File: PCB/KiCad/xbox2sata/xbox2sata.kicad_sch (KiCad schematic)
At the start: 47 parts, among them J1 929975-01-20-RK, J2 61203921621, J3 SATA-A-PL-SMT-K, U1 1V2 voltage regulator, U5 88SA8052, Y1 25MHz

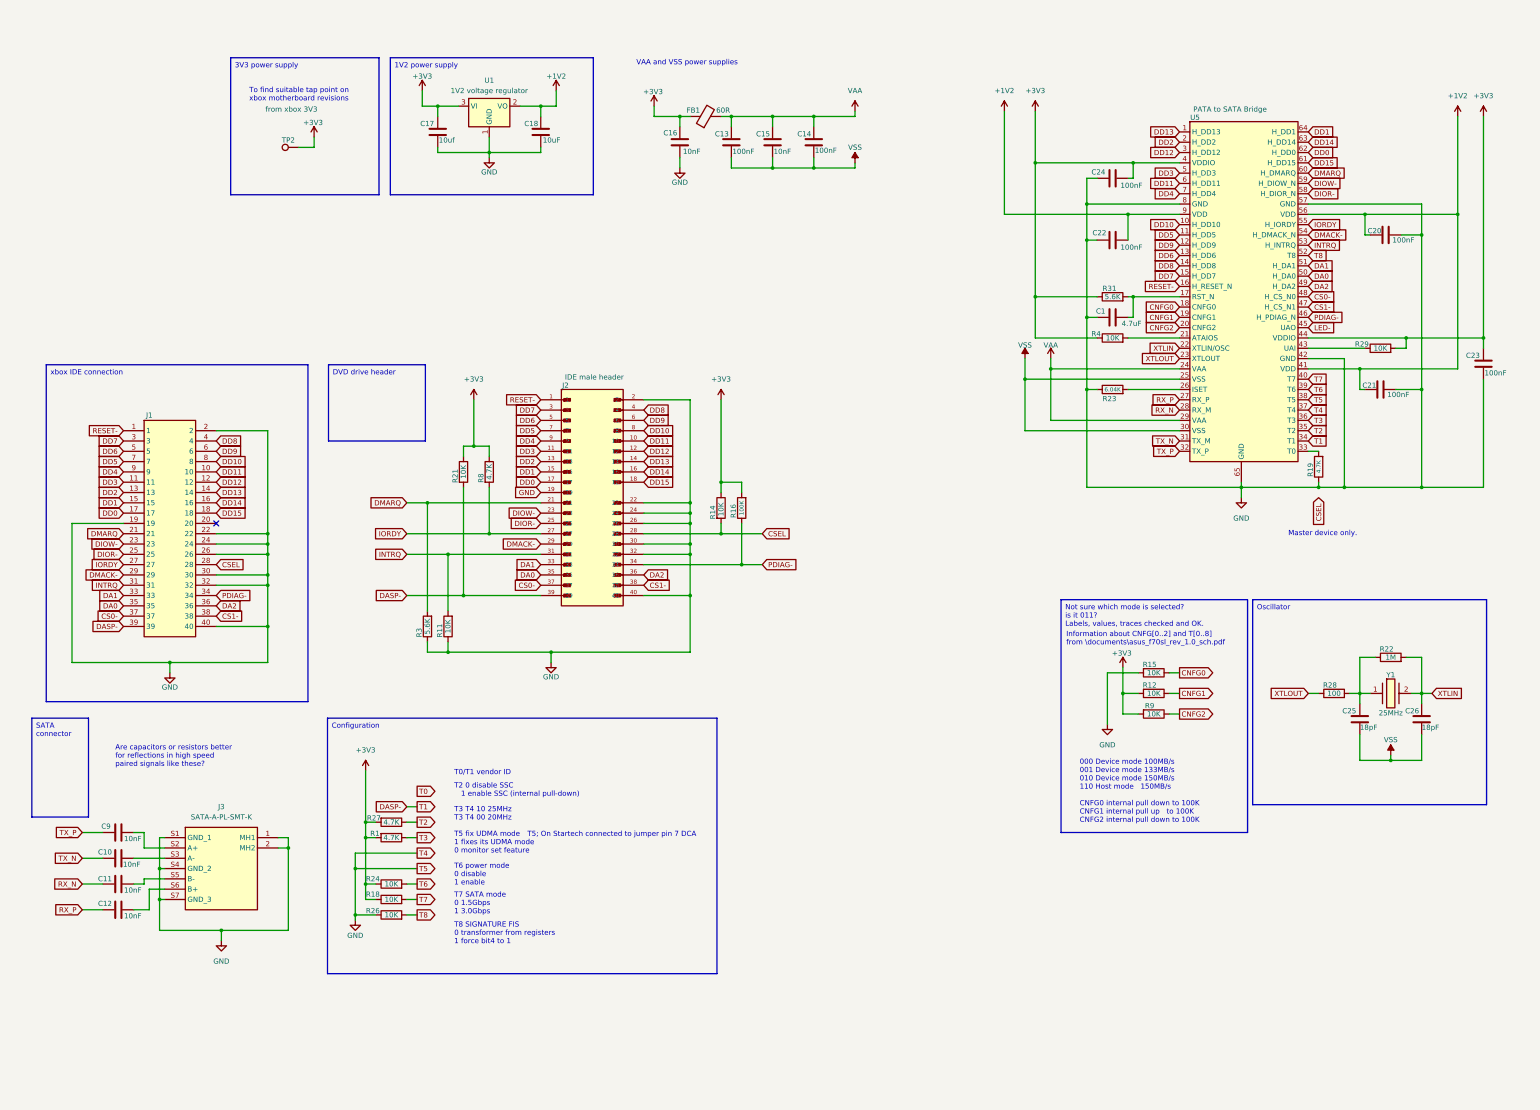
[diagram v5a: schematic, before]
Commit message: Reset-Negative was not enabled
10K resistor (R14) pull-up to 3V3 added to CSEL IDE pin 28
4.7K resistor (R19) pull-down to ground on T0 U5 pin 33 to device as IDE master
Positive power supply icons changed from Global labels to Power symbols

Via sizes changed to 0.3 and 0.5 mm for jlcpcb requirements
Bill of materials updated
Mouser shared basket created;
https://www.mouser.co.uk/api/CrossDomain/GetContext?syncDomains=www&returnUrl=https%3a%2f%2fwww.mouser.com%2fProjectManager%2fProjectDetail.aspx%3fAccessID%3da2276a8976&async=False&setPrefSub=False&clearPrefSub=False
Datasheets added
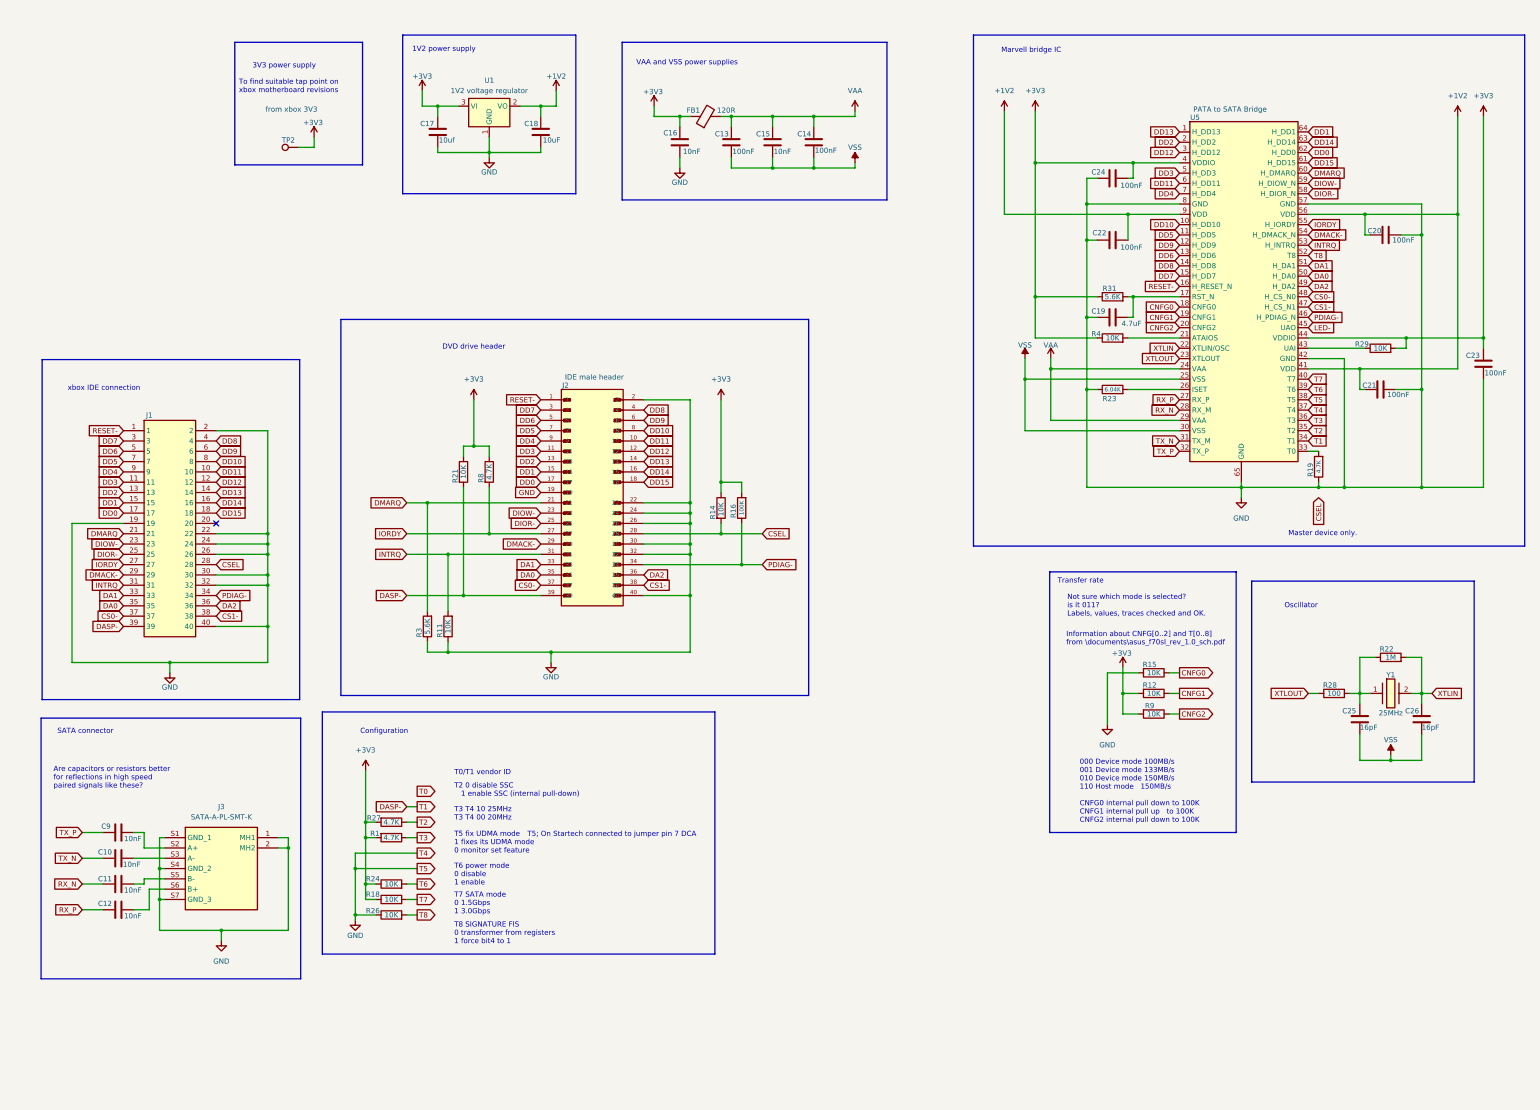
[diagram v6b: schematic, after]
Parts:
- C10, C11, C12, C9: footprint Resistor_SMD:R_0402_1005Metric_Pad0.72x0.64mm_HandSolder -> Capacitor_SMD:C_0402_1005Metric_Pad0.74x0.62mm_HandSolder
- C17, C18: footprint Capacitor_SMD:C_0603_1608Metric_Pad1.08x0.95mm_HandSolder -> Capacitor_SMD:C_0805_2012Metric
- C25, C26: value 18pF -> 16pF
- FB1: value 60R -> 120R; footprint Resistor_SMD:R_0402_1005Metric_Pad0.72x0.64mm_HandSolder -> Inductor_SMD:L_0603_1608Metric; Current rating (none) -> 2A; Frequency (none) -> 100Mhz
- renumbered C1 to C19
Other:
- note added: "1V2 power supply"
- note added: "3V3 power supply"
- note added: "Configuration"
- note added: "DVD drive header"
- note added: "Marvell bridge IC"
- note added: "Not sure which mode is selected? is it 011? Labels, values, traces checked and OK."
- note added: "Oscillator"
- note added: "SATA connector"
- note added: "Transfer rate"
- note added: "xbox IDE connection"
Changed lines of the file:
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@@
 		)
 	)
-	(text_box "Configuration"
-		(exclude_from_sim yes)
-		(at 103.632 187.706 0)
-		(size 96.012 62.992)
+	(rectangle
+		(start 33.274 99.314)
+		(end 96.774 183.134)
 		(stroke
 			(width 0)
@@
 			(type none)
 		)
-		(effects
-			(font
-				(face "Consolas")
-				(size 1.27 1.27)
-			)
-			(justify left top)
-		)
 	)
-	(text_box "1V2 power supply"
-		(exclude_from_sim no)
-		(at 119.126 24.892 0)
-		(size 50.038 33.782)
+	(rectangle
+		(start 331.47 153.924)
+		(end 386.334 203.454)
 		(stroke
 			(width 0)
@@
 			(type none)
 		)
-		(effects
-			(font
-				(face "Consolas")
-				(size 1.27 1.27)
-			)
-			(justify left top)
-		)
 	)
-	(text_box "3V3 power supply"
-		(exclude_from_sim no)
-		(at 79.756 24.892 0)
-		(size 36.576 33.782)
+	(rectangle
+		(start 33.02 187.706)
+		(end 97.028 251.968)
 		(stroke
 			(width 0)
@@
 			(type none)
 		)
-		(effects
-			(font
-				(face "Consolas")
-				(size 1.27 1.27)
-			)
-			(justify left top)
-		)
 	)
-	(text_box "SATA connector"
-		(exclude_from_sim no)
-		(at 30.734 187.706 0)
-		(size 13.97 24.384)
+	(rectangle
+		(start 262.89 19.304)
+		(end 398.78 145.288)
 		(stroke
 			(width 0)
@@
 			(type none)
 		)
-		(effects
-			(font
-				(face "Consolas")
-				(size 1.27 1.27)
-			)
-			(justify left top)
-		)
 	)
-	(text_box "DVD drive header"
-		(exclude_from_sim no)
-		(at 103.886 100.584 0)
-		(size 23.876 18.796)
+	(rectangle
+		(start 80.772 21.082)
+		(end 112.268 51.308)
 		(stroke
 			(width 0)
@@
 			(type none)
 		)
-		(effects
-			(font
-				(face "Consolas")
-				(size 1.27 1.27)
-			)
-			(justify left top)
-		)
 	)
-	(text_box "Oscillator"
-		(exclude_from_sim no)
-		(at 331.724 158.496 0)
-		(size 57.658 50.546)
+	(rectangle
+		(start 106.934 89.408)
+		(end 222.25 182.118)
 		(stroke
 			(width 0)
@@
 			(type none)
 		)
-		(effects
-			(font
-				(face "Consolas")
-				(size 1.27 1.27)
-			)
-			(justify left top)
-		)
 	)
-	(text_box "000 Device mode 100MB/s\n001 Device mode 133MB/s\n010 Device mode 150MB/s\n110 Host mode   150MB/s\n\nCNFG0 internal pull down to 100K\nCNFG1 internal pull up   to 100K\nCNFG2 internal pull down to 100K"
-		(exclude_from_sim no)
-		(at 288.036 196.596 0)
-		(size 38.862 18.034)
+	(rectangle
+		(start 102.362 186.182)
+		(end 199.136 245.872)
 		(stroke
-			(width -0.0001)
+			(width 0)
 			(type default)
 		)
@@
 			(type none)
 		)
-		(effects
-			(font
-				(face "Consolas")
-				(size 1.27 1.27)
-			)
-			(justify left top)
-		)
 	)
-	(text_box "xbox IDE connection"
-		(exclude_from_sim yes)
-		(at 34.29 100.584 0)
-		(size 64.516 83.058)
+	(rectangle
+		(start 281.686 151.638)
+		(end 327.66 215.9)
 		(stroke
 			(width 0)
@@
 			(type none)
 		)
-		(effects
-			(font
-				(face "Consolas")
-				(size 1.27 1.27)
-			)
-			(justify left top)
+	)
+	(rectangle
+		(start 176.276 21.082)
+		(end 241.554 59.944)
+		(stroke
+			(width 0)
+			(type default)
+		)
+		(fill
+			(type none)
 		)
 	)
-	(text_box "Not sure which mode is selected? \nis it 011?\nLabels, values, traces checked and OK."
-		(exclude_from_sim yes)
-		(at 284.48 158.496 0)
-		(size 45.974 57.404)
+	(rectangle
+		(start 122.174 19.304)
+		(end 164.846 58.42)
 		(stroke
 			(width 0)
@@
 			(type none)
 		)
+	)
+	(text_box "000 Device mode 100MB/s\n001 Device mode 133MB/s\n010 Device mode 150MB/s\n110 Host mode   150MB/s\n\nCNFG0 internal pull down to 100K\nCNFG1 internal pull up   to 100K\nCNFG2 internal pull down to 100K"
+		(exclude_from_sim no)
+		(at 288.036 196.596 0)
+		(size 38.862 18.034)
+		(stroke
+			(width -0.0001)
+			(type default)
+		)
+		(fill
+			(type none)
+		)
 		(effects
 			(font
@@
 		)
 	)
+	(text "xbox IDE connection"
+		(exclude_from_sim no)
+		(at 48.514 106.426 0)
+		(effects
+			(font
+				(face "Consolas")
+				(size 1.27 1.27)
+			)
+		)
+	)
 	(text "T5 fix UDMA mode\n1 fixes its UDMA mode\n0 monitor set feature"
 		(exclude_from_sim no)
@@
 		)
 	)
+	(text "DVD drive header"
+		(exclude_from_sim no)
+		(at 139.7 96.266 0)
+		(effects
+			(font
+				(face "Consolas")
+				(size 1.27 1.27)
+			)
+		)
+	)
+	(text "SATA connector"
+		(exclude_from_sim no)
+		(at 43.942 191.008 0)
+		(effects
+			(font
+				(face "Consolas")
+				(size 1.27 1.27)
+			)
+		)
+	)
 	(text "T5; On Startech connected to jumper pin 7 DCA"
 		(exclude_from_sim no)
@@
 		)
 	)
+	(text "Configuration"
+		(exclude_from_sim no)
+		(at 117.602 191.008 0)
+		(effects
+			(font
+				(face "Consolas")
+				(size 1.27 1.27)
+			)
+		)
+	)
 	(text "T7 SATA mode\n0 1.5Gbps\n1 3.0Gbps"
 		(exclude_from_sim no)
@@
 		)
 	)
+	(text "3V3 power supply"
+		(exclude_from_sim no)
+		(at 92.964 26.924 0)
+		(effects
+			(font
+				(face "Consolas")
+				(size 1.27 1.27)
+			)
+		)
+	)
+	(text "Marvell bridge IC"
+		(exclude_from_sim no)
+		(at 277.114 23.114 0)
+		(effects
+			(font
+				(face "Consolas")
+				(size 1.27 1.27)
+			)
+		)
+	)
 	(text "To find suitable tap point on \nxbox motherboard revisions"
 		(exclude_from_sim no)
-		(at 84.328 34.036 0)
+		(at 81.788 32.004 0)
 		(effects
 			(font
@@
 		)
 	)
+	(text "1V2 power supply"
+		(exclude_from_sim no)
+		(at 132.334 22.86 0)
+		(effects
+			(font
+				(face "Consolas")
+				(size 1.27 1.27)
+			)
+		)
+	)
 	(text "Are capacitors or resistors better\nfor reflections in high speed\npaired signals like these?"
 		(exclude_from_sim no)
-		(at 51.308 197.104 0)
+		(at 36.068 202.438 0)
 		(effects
 			(font
@@
 		)
 	)
+	(text "Oscillator"
+		(exclude_from_sim no)
+		(at 343.662 160.02 0)
+		(effects
+			(font
+				(face "Consolas")
+				(size 1.27 1.27)
+			)
+		)
+	)
 	(text "T2 0 disable SSC\n   1 enable SSC (internal pull-down)"
 		(exclude_from_sim no)
@@
 		)
 	)
+	(text "Transfer rate"
+		(exclude_from_sim no)
+		(at 289.306 153.924 0)
+		(effects
+			(font
+				(face "Consolas")
+				(size 1.27 1.27)
+			)
+		)
+	)
 	(text "T8 SIGNATURE FIS\n0 transformer from registers\n1 force bit4 to 1"
 		(exclude_from_sim no)
@@
 		)
 	)
+	(text "Not sure which mode is selected? \nis it 011?\nLabels, values, traces checked and OK."
+		(exclude_from_sim no)
+		(at 286.004 160.02 0)
+		(effects
+			(font
+				(face "Consolas")
+				(size 1.27 1.27)
+			)
+			(justify left)
+		)
+	)
 	(global_label "DA1"
 		(shape input)
@@
 			)
 		)
-		(property "Footprint" "Capacitor_SMD:C_0603_1608Metric_Pad1.08x0.95mm_HandSolder"
+		(property "Footprint" "Capacitor_SMD:C_0805_2012Metric"
 			(at 157.1752 46.99 0)
 			(effects
@@
 			)
 		)
-		(property "Value" "18pF"
+		(property "Value" "16pF"
 			(at 373.38 189.992 0)
 			(effects
@@
 			)
 		)
-		(property "Value" "18pF"
+		(property "Value" "16pF"
 			(at 358.14 189.992 0)
 			(effects
@@
 			)
 		)
-		(property "Footprint" "Resistor_SMD:R_0402_1005Metric_Pad0.72x0.64mm_HandSolder"
+		(property "Footprint" "Capacitor_SMD:C_0402_1005Metric_Pad0.74x0.62mm_HandSolder"
 			(at 55.88 214.9348 0)
 			(effects
@@
 			)
 		)
-		(property "Footprint" "Resistor_SMD:R_0402_1005Metric_Pad0.72x0.64mm_HandSolder"
+		(property "Footprint" "Capacitor_SMD:C_0402_1005Metric_Pad0.74x0.62mm_HandSolder"
 			(at 55.88 227.6348 0)
 			(effects
@@
 			)
 		)
-		(property "Footprint" "Resistor_SMD:R_0402_1005Metric_Pad0.72x0.64mm_HandSolder"
+		(property "Footprint" "Capacitor_SMD:C_0402_1005Metric_Pad0.74x0.62mm_HandSolder"
 			(at 55.88 221.2848 0)
 			(effects
@@
 			)
 		)
-		(property "Value" "60R"
-			(at 201.168 37.846 90)
+		(property "Value" "120R"
+			(at 201.93 37.846 90)
 			(effects
 				(font
@@
 			)
 		)
-		(property "Footprint" "Resistor_SMD:R_0402_1005Metric_Pad0.72x0.64mm_HandSolder"
+		(property "Footprint" "Inductor_SMD:L_0603_1608Metric"
 			(at 196.85 41.148 90)
 			(effects
@@
 			)
 		)
+		(property "Frequency" "100Mhz"
+			(at 196.85 39.37 90)
+			(effects
+				(font
+					(size 1.27 1.27)
+				)
+				(hide yes)
+			)
+		)
+		(property "Current rating" "2A"
+			(at 196.85 39.37 90)
+			(effects
+				(font
+					(size 1.27 1.27)
+				)
+				(hide yes)
+			)
+		)
 		(pin "2"
 		)
@@
 		(on_board yes)
 		(dnp no)
-		(property "Reference" "C1"
+		(property "Reference" "C19"
 			(at 295.402 87.376 90)
 			(effects
@@
 			(project "xbox2sata"
 				(path "/29cbf96f-e8a1-446a-9b4f-b577bf6e6f05"
-					(reference "C1")
+					(reference "C19")
 					(unit 1)
 				)
@@
 			)
 		)
-		(property "Footprint" "Capacitor_SMD:C_0603_1608Metric_Pad1.08x0.95mm_HandSolder"
+		(property "Footprint" "Capacitor_SMD:C_0805_2012Metric"
 			(at 131.7752 39.37 0)
 			(effects
@@
 			)
 		)
-		(property "Footprint" "Resistor_SMD:R_0402_1005Metric_Pad0.72x0.64mm_HandSolder"
+		(property "Footprint" "Capacitor_SMD:C_0402_1005Metric_Pad0.74x0.62mm_HandSolder"
 			(at 55.88 233.9848 0)
 			(effects

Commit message: Two resistors removed, two component values changed
R27 : T2
Not installed, removed

R1 : T3
From 4.7K to 10K

R24 : T6
Not installed, removed

R31 change from 5.6K to 1M
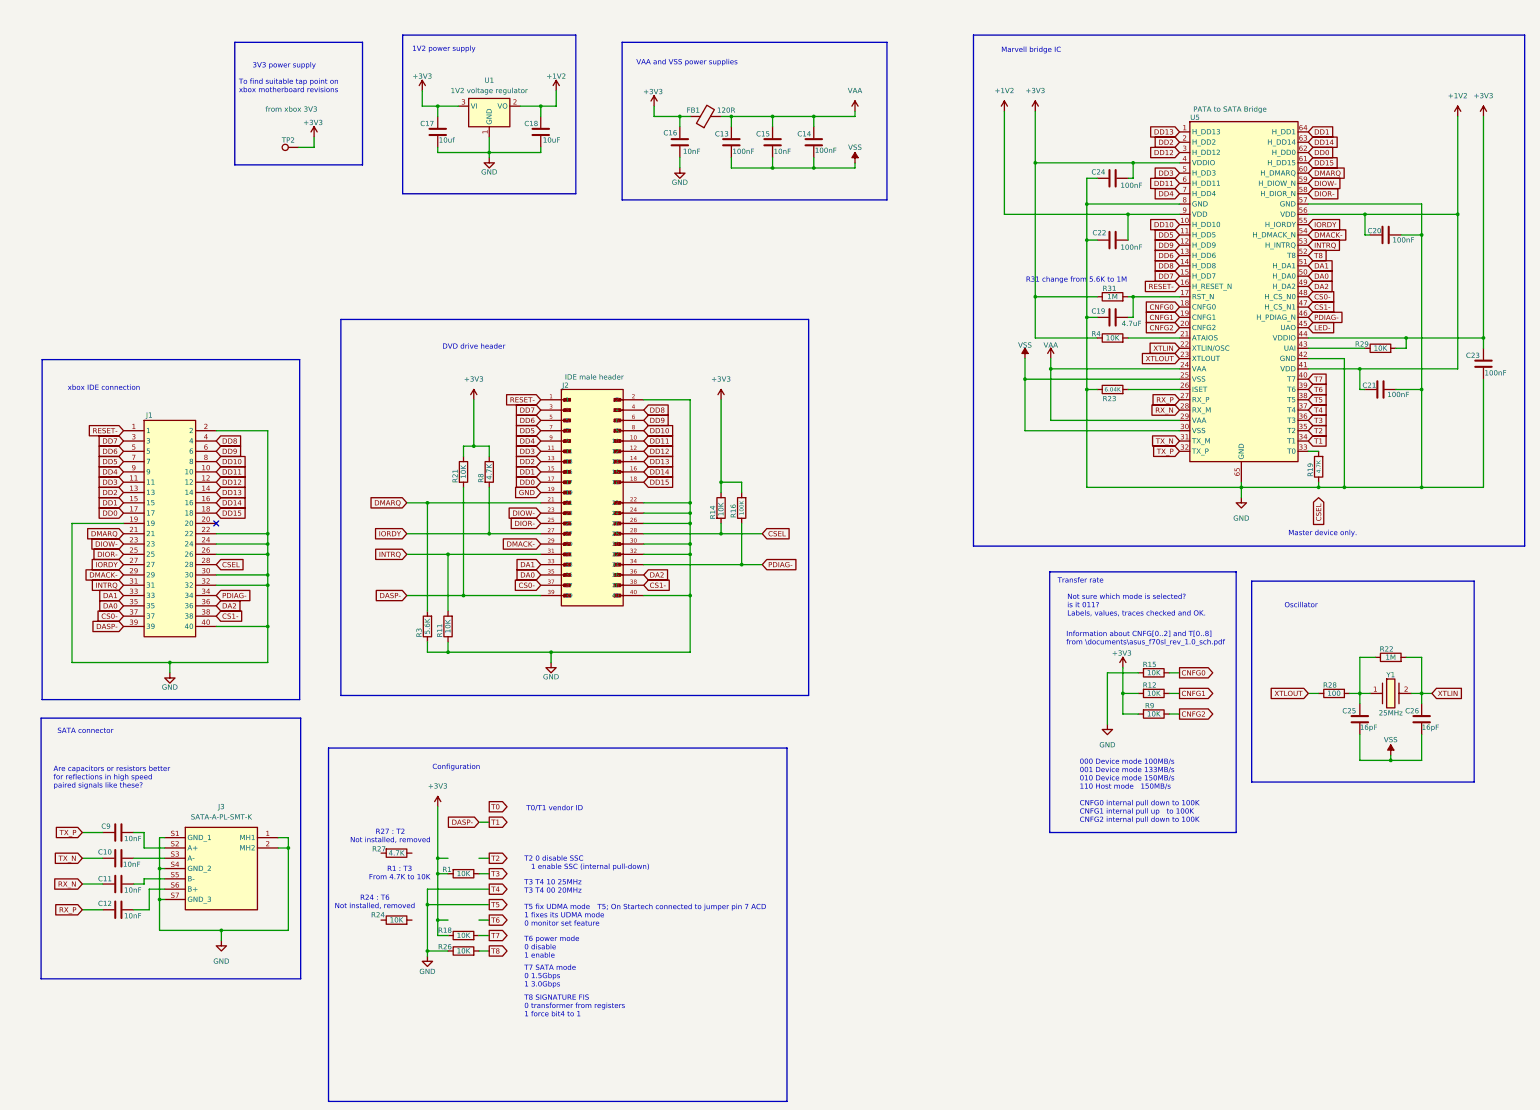
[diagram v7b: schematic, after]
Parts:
- R1: value 4.7K -> 10K
- R31: value 5.6K -> 1M
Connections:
- net +3V3: no longer R24.1, R27.2
- net T2: no longer R27.1
- net T6: no longer R24.2
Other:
- note added: "R1 : T3 From 4.7K to 10K"
- note added: "R24 : T6 Not installed, removed"
- note added: "R27 : T2 Not installed, removed"
- note added: "R31 change from 5.6K to 1M"
- note added: "T5; On Startech connected to jumper pin 7 ACD"
- note removed: "T5; On Startech connected to jumper pin 7 DCA"
- moved on the sheet: R1, R18, R24, R26, R27
